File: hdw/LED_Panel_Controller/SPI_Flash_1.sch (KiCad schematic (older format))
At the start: 14 parts, among them U2501 74LVC1G97, U2502 SST25VF080B-50-4I-S2AF

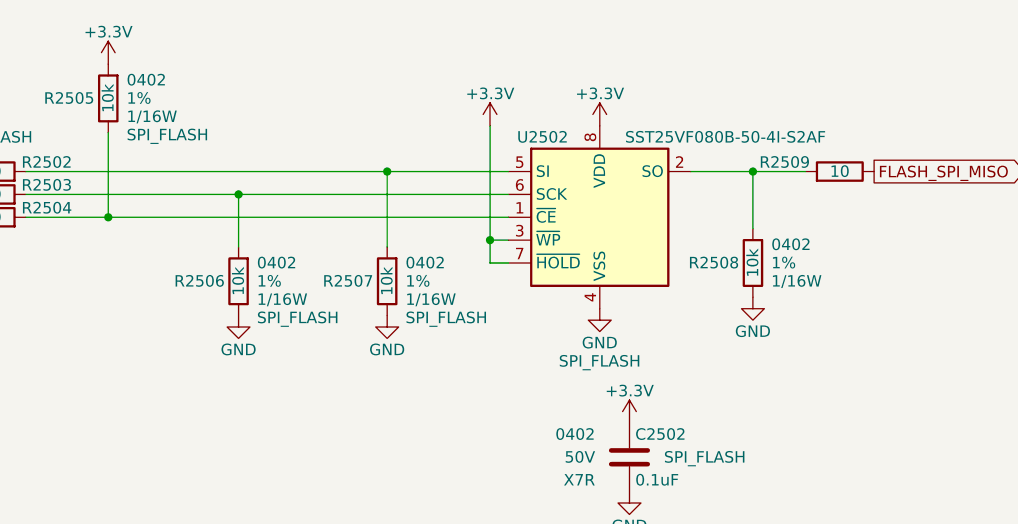
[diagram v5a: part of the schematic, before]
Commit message: fixed SPI flash pull resistors, more PCB placement
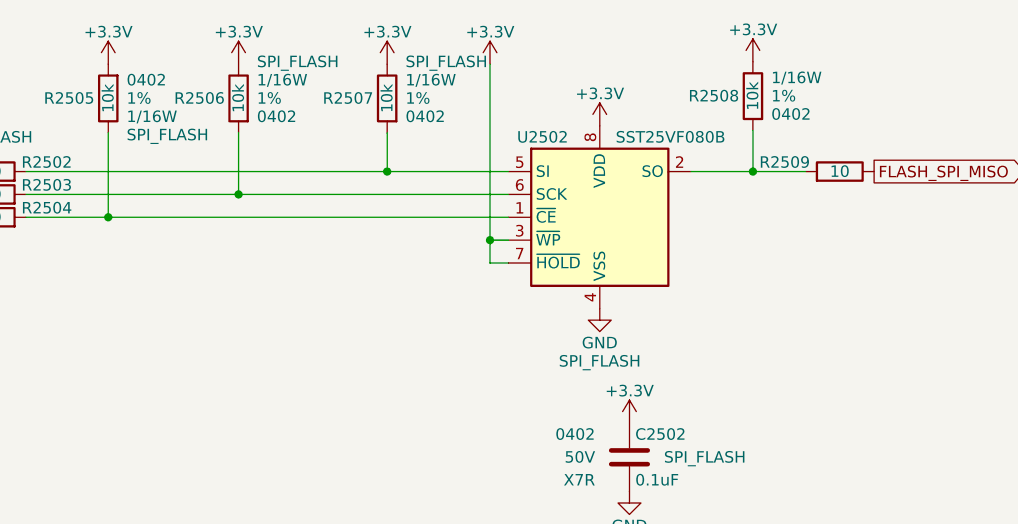
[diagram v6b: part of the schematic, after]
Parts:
- U2502: value SST25VF080B-50-4I-S2AF -> SST25VF080B
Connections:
- net +3V3: now also R2506.2, R2507.2, R2508.2
- net GND: no longer R2506.2, R2507.2, R2508.2
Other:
- moved on the sheet: R2506, R2507, R2508
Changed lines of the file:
@@
 L Custom_Library:R_Custom R2508
 U 1 1 5BB4EDD1
-P 6750 3850
-F 0 "R2508" H 6690 3850 50  0000 R CNN
-F 1 "10k" V 6750 3850 50  0000 C CNN
-F 2 "Resistors_SMD:R_0402" H 6750 3850 50  0001 C CNN
-F 3 "" H 6750 3850 50  0001 C CNN
-F 4 "0402" H 6830 3930 50  0000 L CNN "display_footprint"
-F 5 "1%" H 6830 3850 50  0000 L CNN "Tolerance"
-F 6 "1/16W" H 6830 3770 50  0000 L CNN "Wattage"
-F 7 "RMCF0402FT10K0CT-ND" H 7050 4250 60  0001 C CNN "Digi-Key PN"
-	1    6750 3850
-	1    0    0    -1
-$EndComp
-$Comp
-L power:GND #PWR02508
-U 1 1 5BB4EE63
-P 5150 4080
-F 0 "#PWR02508" H 5150 3830 50  0001 C CNN
-F 1 "GND" H 5150 3930 50  0000 C CNN
-F 2 "" H 5150 4080 50  0001 C CNN
-F 3 "" H 5150 4080 50  0001 C CNN
-	1    5150 4080
-	1    0    0    -1
-$EndComp
-$Comp
-L power:GND #PWR02514
-U 1 1 60786274
-P 6750 4000
-F 0 "#PWR02514" H 6750 3750 50  0001 C CNN
-F 1 "GND" H 6750 3850 50  0000 C CNN
-F 2 "" H 6750 4000 50  0001 C CNN
-F 3 "" H 6750 4000 50  0001 C CNN
-	1    6750 4000
-	1    0    0    -1
+P 6750 3120
+F 0 "R2508" H 6690 3120 50  0000 R CNN
+F 1 "10k" V 6750 3120 50  0000 C CNN
+F 2 "Resistors_SMD:R_0402" H 6750 3120 50  0001 C CNN
+F 3 "" H 6750 3120 50  0001 C CNN
+F 4 "0402" H 6830 3200 50  0000 L CNN "display_footprint"
+F 5 "1%" H 6830 3120 50  0000 L CNN "Tolerance"
+F 6 "1/16W" H 6830 3040 50  0000 L CNN "Wattage"
+F 7 "RMCF0402FT10K0CT-ND" H 7050 3520 60  0001 C CNN "Digi-Key PN"
+	1    6750 3120
+	1    0    0    1
 $EndComp
 $Comp
@@
 $EndComp
 Wire Wire Line
-	5150 3450 5150 3780
-Connection ~ 5150 3450
-Wire Wire Line
-	5150 3450 5680 3450
-Wire Wire Line
 	3930 3280 3930 3650
 Wire Wire Line
 	3930 3650 5680 3650
 Connection ~ 3930 3650
-Wire Wire Line
-	6980 3450 6750 3450
-Wire Wire Line
-	6750 3700 6750 3450
-Connection ~ 6750 3450
-Wire Wire Line
-	6750 3450 6480 3450
 Text GLabel 7280 3450 2    50   Output ~ 0
 FLASH_SPI_MISO
@@
 P 6080 3650
 F 0 "U2502" H 5830 4000 50  0000 C CNN
-F 1 "SST25VF080B-50-4I-S2AF" H 6630 4000 50  0000 C CNN
+F 1 "SST25VF080B" H 6630 4000 50  0000 R CNN
 F 2 "Package_SO:SOIC-8_5.275x5.275mm_P1.27mm" H 6080 2950 50  0001 C CNN
 F 3 "http://ww1.microchip.com/downloads/en/DeviceDoc/20005045C.pdf" H 6030 4200 50  0001 C CNN
@@
 L power:+3.3V #PWR02509
 U 1 1 6078630D
-P 5600 3250
-F 0 "#PWR02509" H 5600 3100 50  0001 C CNN
-F 1 "+3.3V" H 5600 3390 50  0000 C CNN
-F 2 "" H 5600 3250 50  0001 C CNN
-F 3 "" H 5600 3250 50  0001 C CNN
-	1    5600 3250
+P 5600 2980
+F 0 "#PWR02509" H 5600 2830 50  0001 C CNN
+F 1 "+3.3V" H 5600 3120 50  0000 C CNN
+F 2 "" H 5600 2980 50  0001 C CNN
+F 3 "" H 5600 2980 50  0001 C CNN
+	1    5600 2980
 	1    0    0    -1
 $EndComp
@@
 	5680 3750 5600 3750
 Wire Wire Line
-	5600 3750 5600 3250
+	5600 3750 5600 2980
 Wire Wire Line
 	5680 3850 5600 3850
@@
 	5600 3850 5600 3750
 Connection ~ 5600 3750
-Wire Wire Line
-	3570 3550 4500 3550
 $Comp
 L Custom_Library:R_Custom R2506
 U 1 1 60786317
-P 4500 3930
-F 0 "R2506" H 4440 3930 50  0000 R CNN
-F 1 "10k" V 4500 3930 50  0000 C CNN
-F 2 "Resistors_SMD:R_0402" H 4500 3930 50  0001 C CNN
-F 3 "" H 4500 3930 50  0001 C CNN
-F 4 "0402" H 4580 4010 50  0000 L CNN "display_footprint"
-F 5 "1%" H 4580 3930 50  0000 L CNN "Tolerance"
-F 6 "1/16W" H 4580 3850 50  0000 L CNN "Wattage"
-F 7 "RMCF0402FT10K0CT-ND" H 4800 4330 60  0001 C CNN "Digi-Key PN"
-F 8 "SPI_FLASH" H 4580 3770 50  0000 L CNN "Configuration"
-	1    4500 3930
-	1    0    0    -1
-$EndComp
-$Comp
-L power:GND #PWR02507
-U 1 1 6078631C
-P 4500 4080
-F 0 "#PWR02507" H 4500 3830 50  0001 C CNN
-F 1 "GND" H 4500 3930 50  0000 C CNN
-F 2 "" H 4500 4080 50  0001 C CNN
-F 3 "" H 4500 4080 50  0001 C CNN
-	1    4500 4080
-	1    0    0    -1
-$EndComp
-Wire Wire Line
-	3570 3450 5150 3450
-Wire Wire Line
-	4500 3550 4500 3780
-Connection ~ 4500 3550
-Wire Wire Line
-	4500 3550 5680 3550
+P 4500 3130
+F 0 "R2506" H 4440 3130 50  0000 R CNN
+F 1 "10k" V 4500 3130 50  0000 C CNN
+F 2 "Resistors_SMD:R_0402" H 4500 3130 50  0001 C CNN
+F 3 "" H 4500 3130 50  0001 C CNN
+F 4 "0402" H 4580 3210 50  0000 L CNN "display_footprint"
+F 5 "1%" H 4580 3130 50  0000 L CNN "Tolerance"
+F 6 "1/16W" H 4580 3050 50  0000 L CNN "Wattage"
+F 7 "RMCF0402FT10K0CT-ND" H 4800 3530 60  0001 C CNN "Digi-Key PN"
+F 8 "SPI_FLASH" H 4580 2970 50  0000 L CNN "Configuration"
+	1    4500 3130
+	1    0    0    1
+$EndComp
 $Comp
 L Custom_Library:R_Custom R2503
@@
 L Custom_Library:R_Custom R2507
 U 1 1 6078635A
-P 5150 3930
-F 0 "R2507" H 5090 3930 50  0000 R CNN
-F 1 "10k" V 5150 3930 50  0000 C CNN
-F 2 "Resistors_SMD:R_0402" H 5150 3930 50  0001 C CNN
-F 3 "" H 5150 3930 50  0001 C CNN
-F 4 "0402" H 5230 4010 50  0000 L CNN "display_footprint"
-F 5 "1%" H 5230 3930 50  0000 L CNN "Tolerance"
-F 6 "1/16W" H 5230 3850 50  0000 L CNN "Wattage"
-F 7 "RMCF0402FT10K0CT-ND" H 5450 4330 60  0001 C CNN "Digi-Key PN"
-F 8 "SPI_FLASH" H 5230 3770 50  0000 L CNN "Configuration"
-	1    5150 3930
-	1    0    0    -1
+P 5150 3130
+F 0 "R2507" H 5090 3130 50  0000 R CNN
+F 1 "10k" V 5150 3130 50  0000 C CNN
+F 2 "Resistors_SMD:R_0402" H 5150 3130 50  0001 C CNN
+F 3 "" H 5150 3130 50  0001 C CNN
+F 4 "0402" H 5230 3210 50  0000 L CNN "display_footprint"
+F 5 "1%" H 5230 3130 50  0000 L CNN "Tolerance"
+F 6 "1/16W" H 5230 3050 50  0000 L CNN "Wattage"
+F 7 "RMCF0402FT10K0CT-ND" H 5450 3530 60  0001 C CNN "Digi-Key PN"
+F 8 "SPI_FLASH" H 5230 2970 50  0000 L CNN "Configuration"
+	1    5150 3130
+	1    0    0    1
 $EndComp
 $Comp
@@
 	1    0    0    -1
 $EndComp
+Wire Wire Line
+	3570 3450 5150 3450
+Wire Wire Line
+	3570 3550 4500 3550
+$Comp
+L power:+3.3V #PWR0106
+U 1 1 6067513C
+P 5150 2980
+F 0 "#PWR0106" H 5150 2830 50  0001 C CNN
+F 1 "+3.3V" H 5150 3120 50  0000 C CNN
+F 2 "" H 5150 2980 50  0001 C CNN
+F 3 "" H 5150 2980 50  0001 C CNN
+	1    5150 2980
+	1    0    0    -1
+$EndComp
+$Comp
+L power:+3.3V #PWR0107
+U 1 1 606753E2
+P 4500 2980
+F 0 "#PWR0107" H 4500 2830 50  0001 C CNN
+F 1 "+3.3V" H 4500 3120 50  0000 C CNN
+F 2 "" H 4500 2980 50  0001 C CNN
+F 3 "" H 4500 2980 50  0001 C CNN
+	1    4500 2980
+	1    0    0    -1
+$EndComp
+Wire Wire Line
+	4500 3280 4500 3550
+Connection ~ 4500 3550
+Wire Wire Line
+	4500 3550 5680 3550
+Wire Wire Line
+	5150 3280 5150 3450
+Connection ~ 5150 3450
+Wire Wire Line
+	5150 3450 5680 3450
+Wire Wire Line
+	6480 3450 6750 3450
+Wire Wire Line
+	6750 3270 6750 3450
+Connection ~ 6750 3450
+Wire Wire Line
+	6750 3450 6980 3450
+$Comp
+L power:+3.3V #PWR0108
+U 1 1 60676A71
+P 6750 2970
+F 0 "#PWR0108" H 6750 2820 50  0001 C CNN
+F 1 "+3.3V" H 6750 3110 50  0000 C CNN
+F 2 "" H 6750 2970 50  0001 C CNN
+F 3 "" H 6750 2970 50  0001 C CNN
+	1    6750 2970
+	1    0    0    -1
+$EndComp

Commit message: added BOMs, some consolidation
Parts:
- C2501, C2502: Digi-Key PN 490-10701-1-ND -> 490-10698-1-ND
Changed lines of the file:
@@
 F 5 "50V" H 1860 6900 50  0000 R CNN "Voltage"
 F 6 "X7R" H 1860 6800 50  0000 R CNN "Dielectric"
-F 7 "490-10701-1-ND" H 2435 7400 60  0001 C CNN "Digi-Key PN"
+F 7 "490-10698-1-ND" H 2435 7400 60  0001 C CNN "Digi-Key PN"
 F 8 "SPI_FLASH" H 2340 6900 50  0000 C CNN "Configuration"
 	1    2010 6900
@@
 F 5 "50V" H 6060 4700 50  0000 R CNN "Voltage"
 F 6 "X7R" H 6060 4600 50  0000 R CNN "Dielectric"
-F 7 "490-10701-1-ND" H 6635 5200 60  0001 C CNN "Digi-Key PN"
+F 7 "490-10698-1-ND" H 6635 5200 60  0001 C CNN "Digi-Key PN"
 F 8 "SPI_FLASH" H 6540 4700 50  0000 C CNN "Configuration"
 	1    6210 4700
